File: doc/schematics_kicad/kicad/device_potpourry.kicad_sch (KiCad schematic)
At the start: 6 parts, among them T1204 tentacle, T1205 tentacle

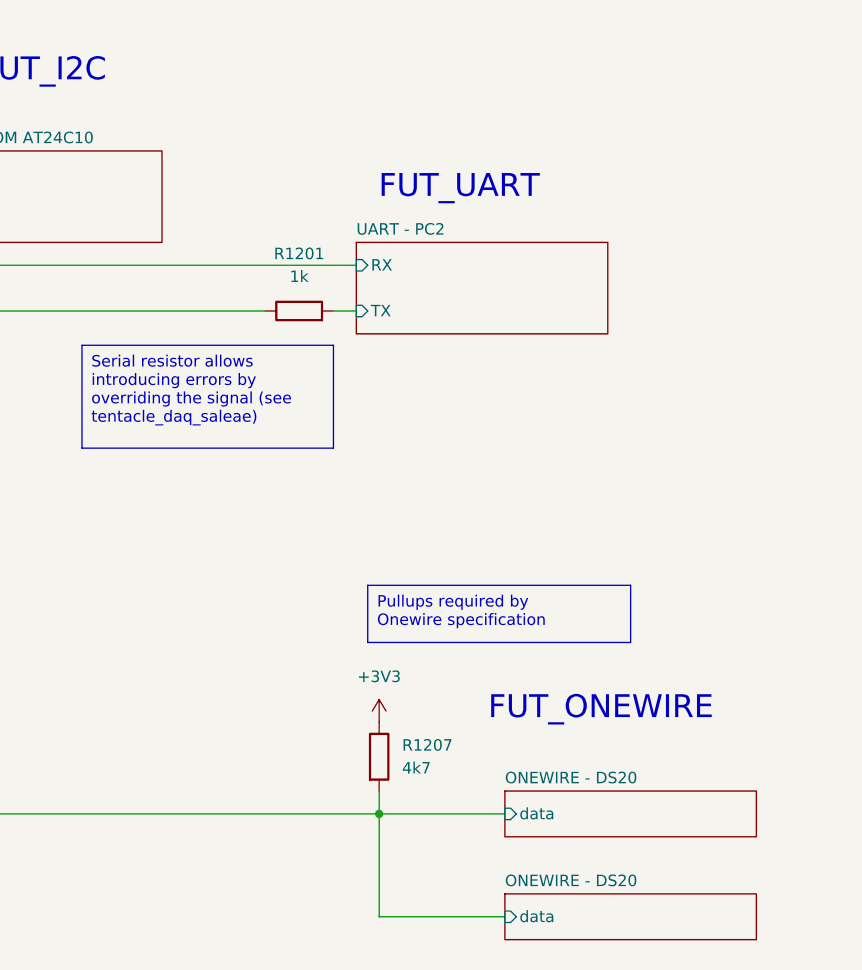
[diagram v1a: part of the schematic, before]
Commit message: MCU names as in micropython-git
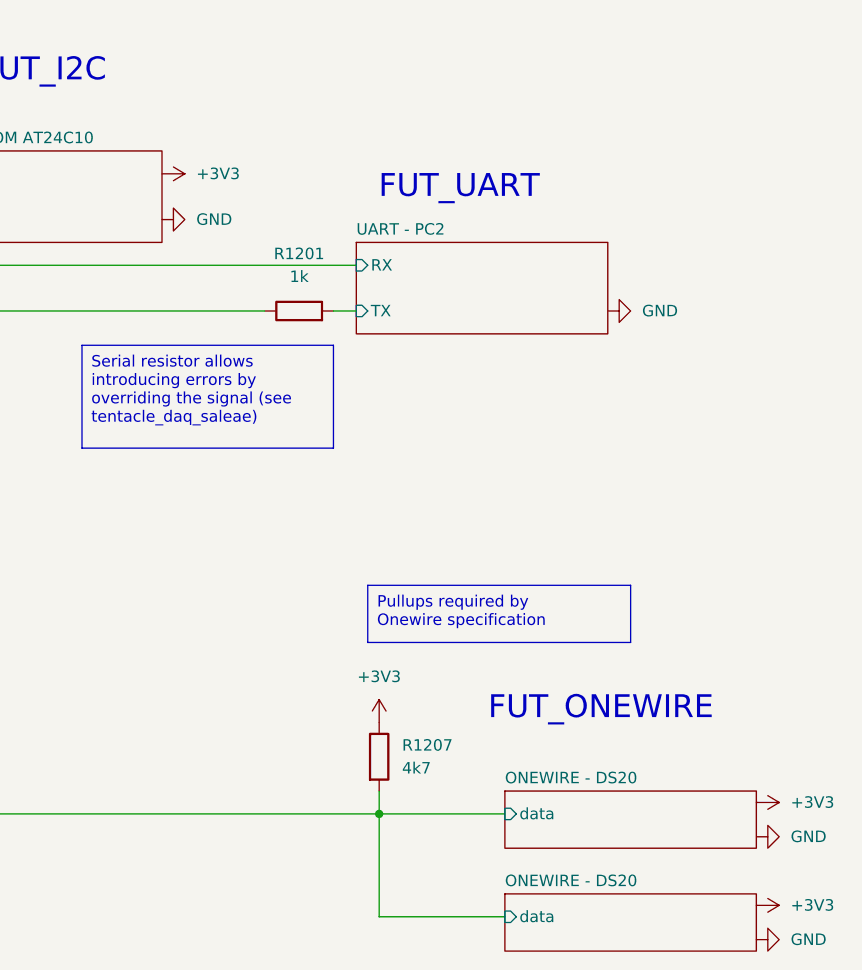
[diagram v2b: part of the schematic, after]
